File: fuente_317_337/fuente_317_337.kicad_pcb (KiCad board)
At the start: 2 copper layers, 80 x 61 mm, 52 parts, among them J1 Fuente, J10 SEL_7905, J11 -5, J12 ADC+, J13 ADC-, J2 Salida, J3 Salida_12v, J4 Cooler, J5 +5, J6 GND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

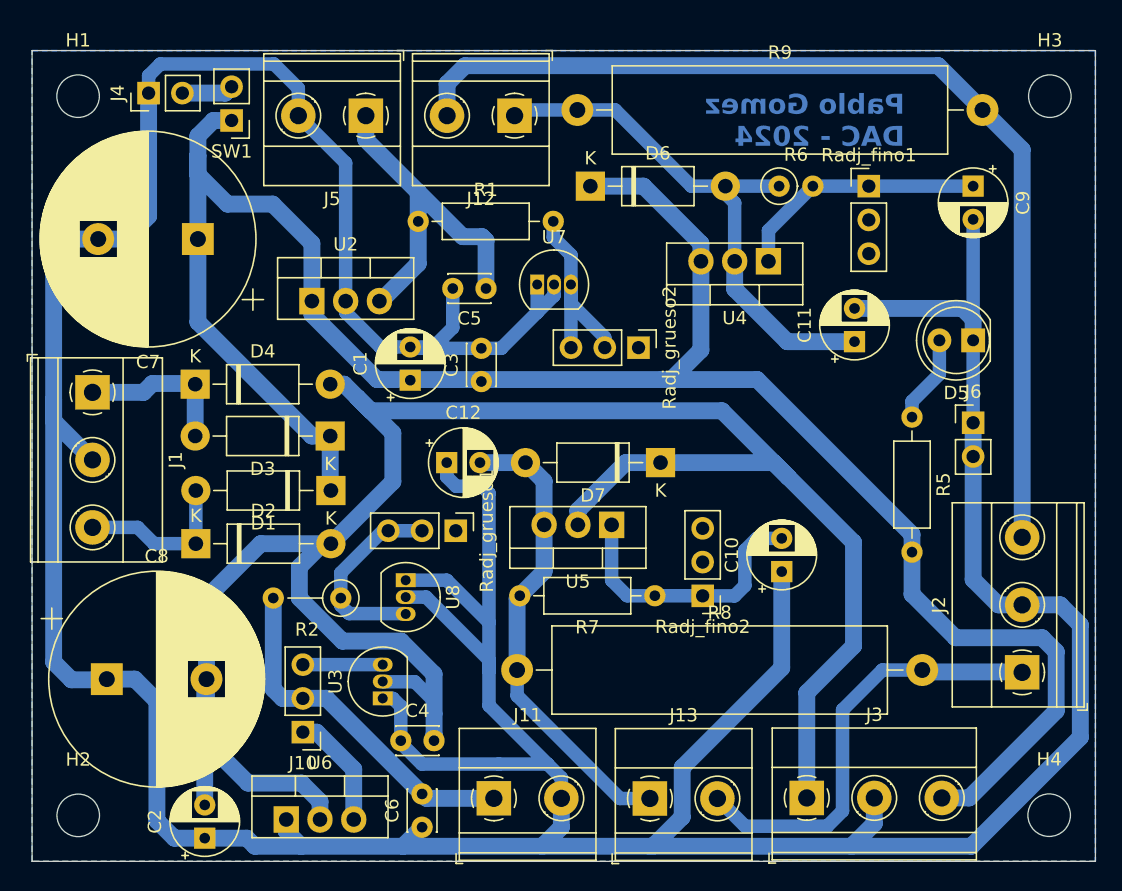
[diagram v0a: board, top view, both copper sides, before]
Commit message: fix ground plane in fuente_317_337
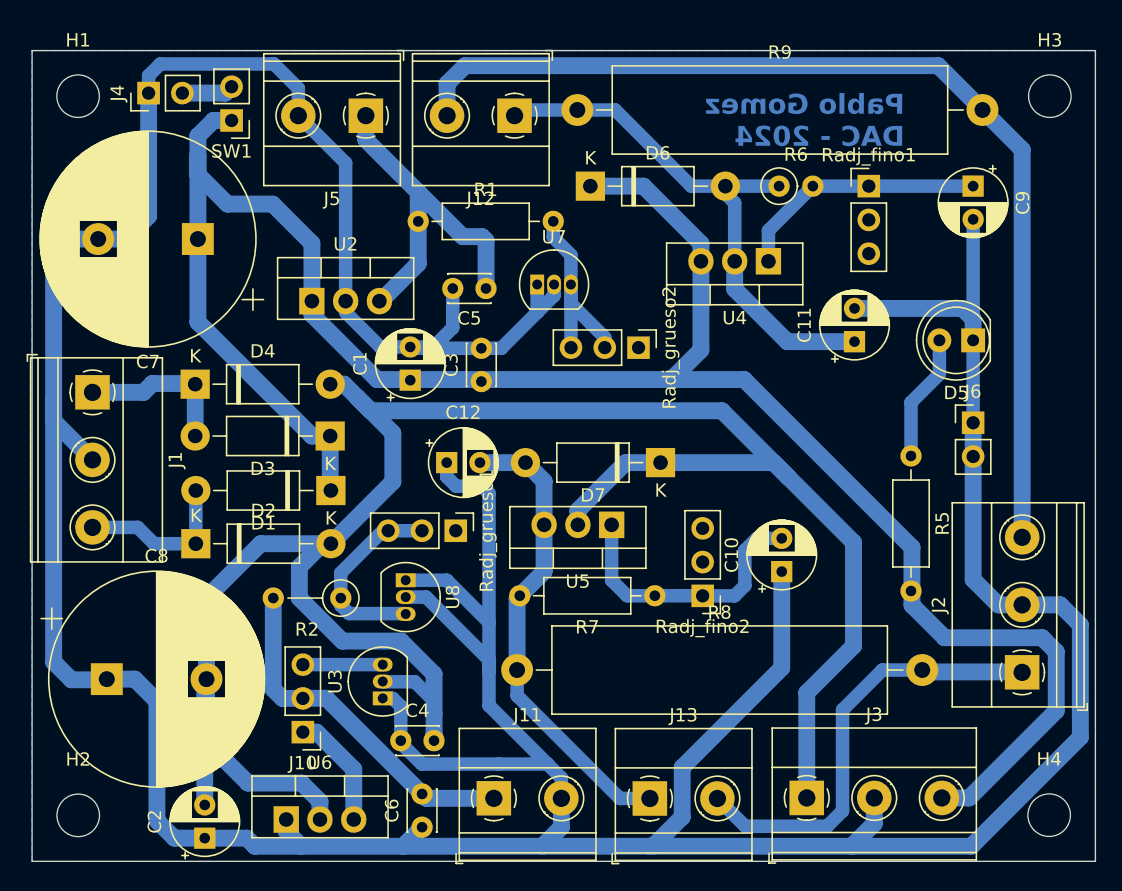
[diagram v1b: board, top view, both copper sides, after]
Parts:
- moved R5 2.93 mm to (86.1, 44.5)
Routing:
- net Net-(D5-A): track 6.63 -> 9.58 mm
- removed copper zone on B.Cu, net (none)
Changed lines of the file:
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@@
 	(footprint "Resistor_THT:R_Axial_DIN0207_L6.3mm_D2.5mm_P10.16mm_Horizontal"
 		(layer "F.Cu")
-		(at 86.2 41.575 -90)
+		(at 86.125 44.5 -90)
 		(descr "Resistor, Axial_DIN0207 series, Axial, Horizontal, pin pitch=10.16mm, 0.25W = 1/4W, length*diameter=6.3*2.5mm^2, http://cdn-reichelt.de/documents/datenblatt/B400/1_4W%23YAG.pdf")
 		(tags "Resistor Axial_DIN0207 series Axial Horizontal pin pitch 10.16mm 0.25W = 1/4W length 6.3mm diameter 2.5mm")
@@
 	)
 	(segment
-		(start 90.495 70.23)
-		(end 97.05 63.675)
+		(start 73.575 38.75)
+		(end 45.95 38.75)
 		(width 1.27)
 		(layer "B.Cu")
@@
 	)
 	(segment
+		(start 86.2 55.725)
+		(end 86.2 51.375)
+		(width 1.27)
+		(layer "B.Cu")
+		(net 2)
+	)
+	(segment
 		(start 33.64 19.26)
 		(end 35.01 19.26)
@@
 	)
 	(segment
-		(start 68.1 38.75)
-		(end 67.4 38.75)
+		(start 97.05 59.2294)
+		(end 95.9956 58.175)
 		(width 1.27)
 		(layer "B.Cu")
@@
 	)
 	(segment
-		(start 74.55 38.75)
-		(end 45.95 38.75)
+		(start 68.1 38.75)
+		(end 67.4 38.75)
 		(width 1.27)
 		(layer "B.Cu")
@@
 	)
 	(segment
-		(start 41.05 33.85)
-		(end 41.05 32.85)
+		(start 45.95 38.75)
+		(end 41.05 33.85)
 		(width 1.27)
 		(layer "B.Cu")
@@
 	)
 	(segment
-		(start 95.9956 58.175)
-		(end 89.475 58.175)
+		(start 90.495 70.23)
+		(end 97.05 63.675)
 		(width 1.27)
 		(layer "B.Cu")
@@
 	)
 	(segment
-		(start 45.95 38.75)
-		(end 41.05 33.85)
+		(start 88.65 58.175)
+		(end 86.2 55.725)
 		(width 1.27)
 		(layer "B.Cu")
@@
 	)
 	(segment
-		(start 97.05 59.2294)
-		(end 95.9956 58.175)
+		(start 88.4428 70.23)
+		(end 90.495 70.23)
+		(width 1.27)
+		(layer "B.Cu")
+		(net 2)
+	)
+	(segment
+		(start 97.05 63.675)
+		(end 97.05 59.2294)
 		(width 1.27)
 		(layer "B.Cu")
@@
 	)
 	(segment
-		(start 88.4428 70.23)
-		(end 90.495 70.23)
+		(start 86.2 51.375)
+		(end 73.575 38.75)
 		(width 1.27)
 		(layer "B.Cu")
@@
 	)
 	(segment
-		(start 86.2 54.9)
-		(end 86.2 50.4)
-		(width 1.27)
-		(layer "B.Cu")
-		(net 2)
-	)
-	(segment
-		(start 89.475 58.175)
-		(end 86.2 54.9)
+		(start 41.05 28.5)
+		(end 41.05 32.85)
 		(width 1.27)
 		(layer "B.Cu")
@@
 	)
 	(segment
-		(start 41.05 28.5)
-		(end 41.05 32.85)
+		(start 95.9956 58.175)
+		(end 88.65 58.175)
 		(width 1.27)
 		(layer "B.Cu")
@@
 	)
 	(segment
-		(start 86.2 50.4)
-		(end 74.55 38.75)
-		(width 1.27)
-		(layer "B.Cu")
-		(net 2)
-	)
-	(segment
 		(start 32.472755 34.422755)
 		(end 32.472755 28.18)
@@
 	)
 	(segment
-		(start 97.05 63.675)
-		(end 97.05 59.2294)
+		(start 70.32 29.855)
+		(end 70.32 36.53)
 		(width 1.27)
 		(layer "B.Cu")
@@
 	)
 	(segment
-		(start 70.32 29.855)
-		(end 70.32 36.53)
+		(start 41.05 33.85)
+		(end 41.05 32.85)
 		(width 1.27)
 		(layer "B.Cu")
@@
 	)
 	(segment
-		(start 86.2 40.4)
-		(end 88.26 38.34)
+		(start 86.125 44.5)
+		(end 86.125 40.475)
 		(width 1.016)
 		(layer "B.Cu")
@@
 	)
 	(segment
-		(start 88.26 38.34)
-		(end 88.26 35.8)
+		(start 86.125 40.475)
+		(end 88.26 38.34)
 		(width 1.016)
 		(layer "B.Cu")
@@
 	)
 	(segment
-		(start 86.2 41.575)
-		(end 86.2 40.4)
+		(start 88.26 38.34)
+		(end 88.26 35.8)
 		(width 1.016)
 		(layer "B.Cu")
@@
 	)
 	(zone
-		(net 0)
-		(net_name "")
-		(layer "B.Cu")
-		(hatch edge 0.5)
-		(priority 1)
-		(connect_pads
-			(clearance 0.5)
-		)
-		(min_thickness 0.25)
-		(filled_areas_thickness no)
-		(fill yes
-			(thermal_gap 0.5)
-			(thermal_bridge_width 0.5)
-			(island_removal_mode 1)
-			(island_area_min 10)
-		)
-		(polygon
-			(pts
-				(xy 20 14) (xy 100 14) (xy 100 75) (xy 20 75)
-			)
-		)
-	)
-	(zone

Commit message: pcb minimal change
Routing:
- net Net-(Radj_fino1-Pad2): track 0.00 -> 48.1 mm
- net Net-(Radj_fino2-Pad2): track 0.00 -> 19.7 mm
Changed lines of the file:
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@@
 		(net 19)
+	)
+	(segment
+		(start 81.55 31.825)
+		(end 82.95 30.425)
+		(width 0.2)
+		(layer "F.Cu")
+		(net 20)
+	)
+	(segment
+		(start 62.7 31.825)
+		(end 81.55 31.825)
+		(width 0.2)
+		(layer "F.Cu")
+		(net 20)
+	)
+	(segment
+		(start 54.9 39.625)
+		(end 62.7 31.825)
+		(width 0.2)
+		(layer "F.Cu")
+		(net 20)
+	)
+	(segment
+		(start 82.95 30.425)
+		(end 82.95 29.28)
+		(width 0.2)
+		(layer "F.Cu")
+		(net 20)
+	)
+	(segment
+		(start 53.3 50.125)
+		(end 54.9 48.525)
+		(width 0.2)
+		(layer "F.Cu")
+		(net 20)
+	)
+	(segment
+		(start 51.875 50.125)
+		(end 53.3 50.125)
+		(width 0.2)
+		(layer "F.Cu")
+		(net 20)
+	)
+	(segment
+		(start 54.9 48.525)
+		(end 54.9 39.625)
+		(width 0.2)
+		(layer "F.Cu")
+		(net 20)
+	)
+	(segment
+		(start 82.95 26.74)
+		(end 82.95 29.28)
+		(width 1.016)
+		(layer "B.Cu")
+		(net 20)
+	)
+	(segment
+		(start 65.625 36.35)
+		(end 68.25 36.35)
+		(width 0.2)
+		(layer "F.Cu")
+		(net 21)
+	)
+	(segment
+		(start 70.45 38.55)
+		(end 70.45 49.945)
+		(width 0.2)
+		(layer "F.Cu")
+		(net 21)
+	)
+	(segment
+		(start 68.25 36.35)
+		(end 70.45 38.55)
+		(width 0.2)
+		(layer "F.Cu")
+		(net 21)
+	)
+	(segment
+		(start 70.45 52.485)
+		(end 70.45 49.945)
+		(width 1.016)
+		(layer "B.Cu")
+		(net 21)
 	)
 	(zone
